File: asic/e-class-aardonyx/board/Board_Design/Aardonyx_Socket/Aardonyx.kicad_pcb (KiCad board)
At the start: 4 copper layers, 329 parts, among them J1 Conn_1x4, J10 Conn_1x3_M, J11 Conn_1x8, J12 Conn_1x3_M, J13 USB_B_6PIN, J14 Conn_1x4, J15 Conn_1x3_M, J16 USB_OTG, J17 Conn_1x8, J18 Conn_1x3_M, J19 Conn_1x3_M, J2 Conn_1x6, J3 Conn_1x10_F, J4 Conn_1x8_F, J5 Conn_1x8_F, J6 Conn_1x6_F, J7 Conn_1x3_M, J8 PJ-202H PWRJACK, J9 Conn_1x6, Q1 FDN339AN, SW1 FSM2JSMAATR, SW2 SW_DIP_x03, SW3 SW_SPST, U1 LSF0108PWR, U10 ADM1186, U11 FT2232H, U12 TPS7A7002DDAR, U13 TPS54627DDAR, U14 93LC56BT-I_OT, U15 TPS7A7002DDAR, U2 SKT32E, U3 IS42S32160F-TSOP2, U4 LSF0108PWR, U5 CDCE913PW, U6 ADC128S102CIMTX/NOPB, U7 74AUP1G09GW, U8 IS25LP256x-xM, U9 CAT24M01WI-GT3, Y1 27MHz, Y2 12MHz

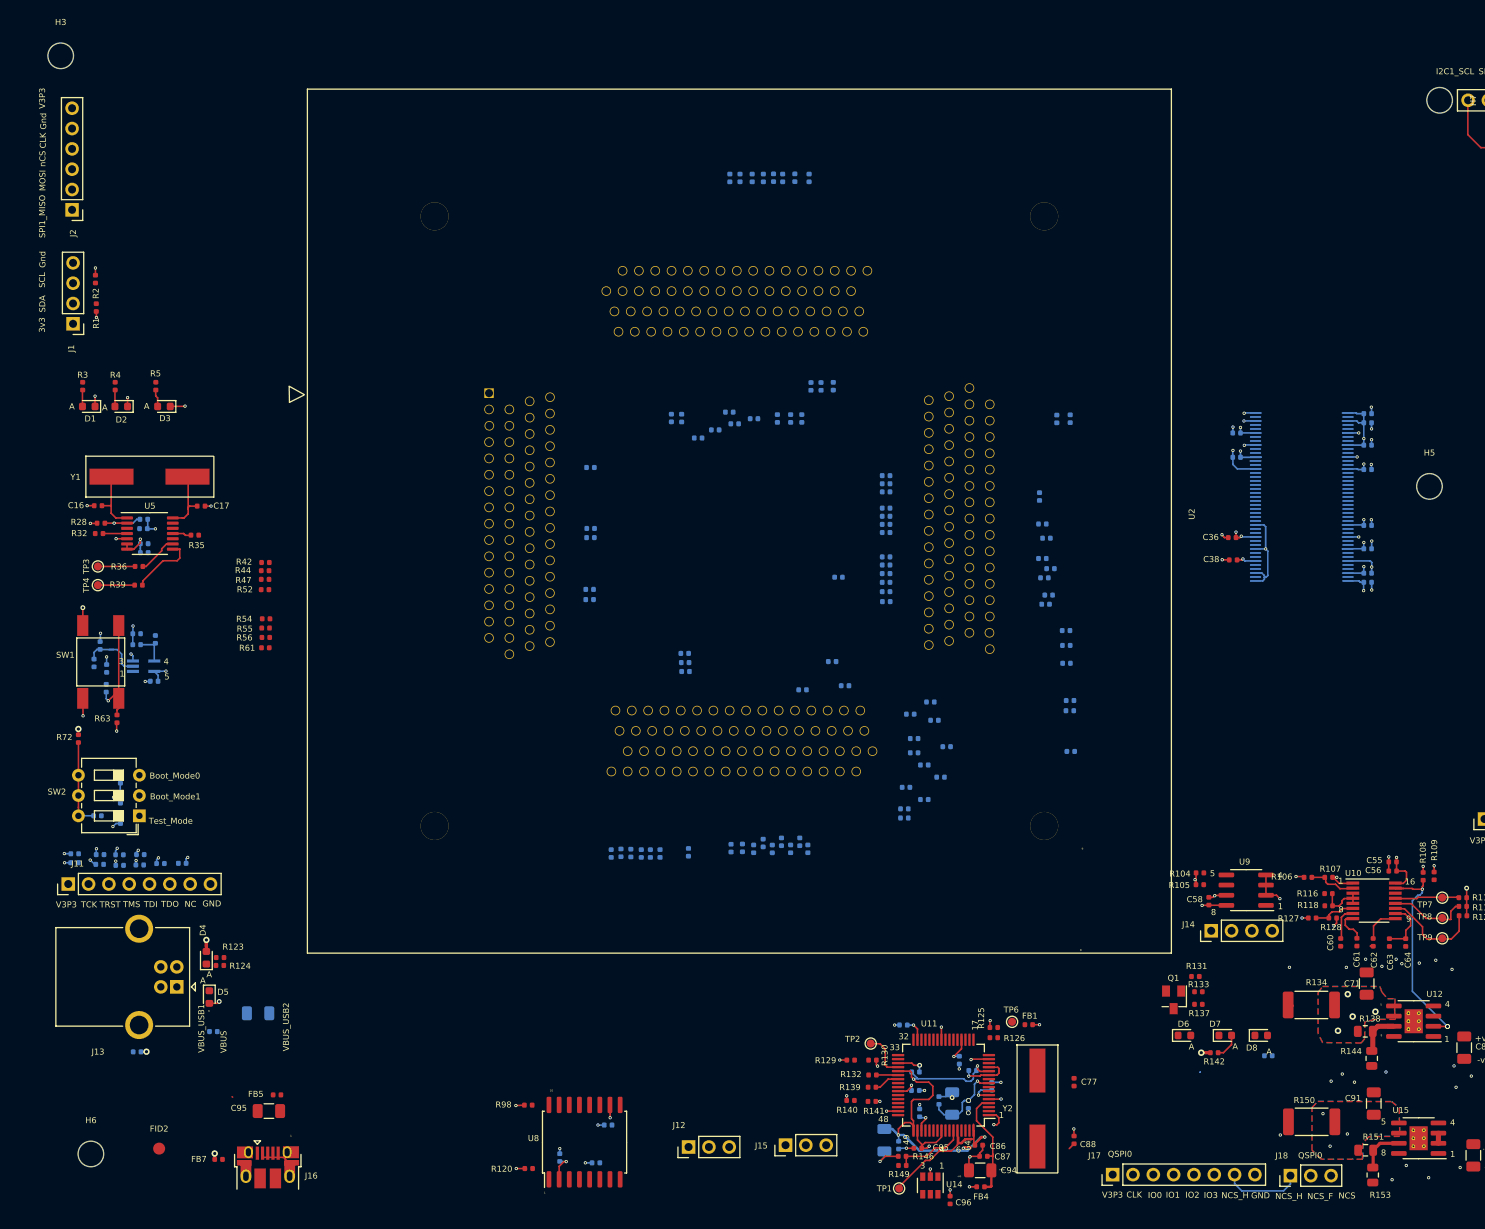
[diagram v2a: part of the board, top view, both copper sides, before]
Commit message: Adding Mounting hole
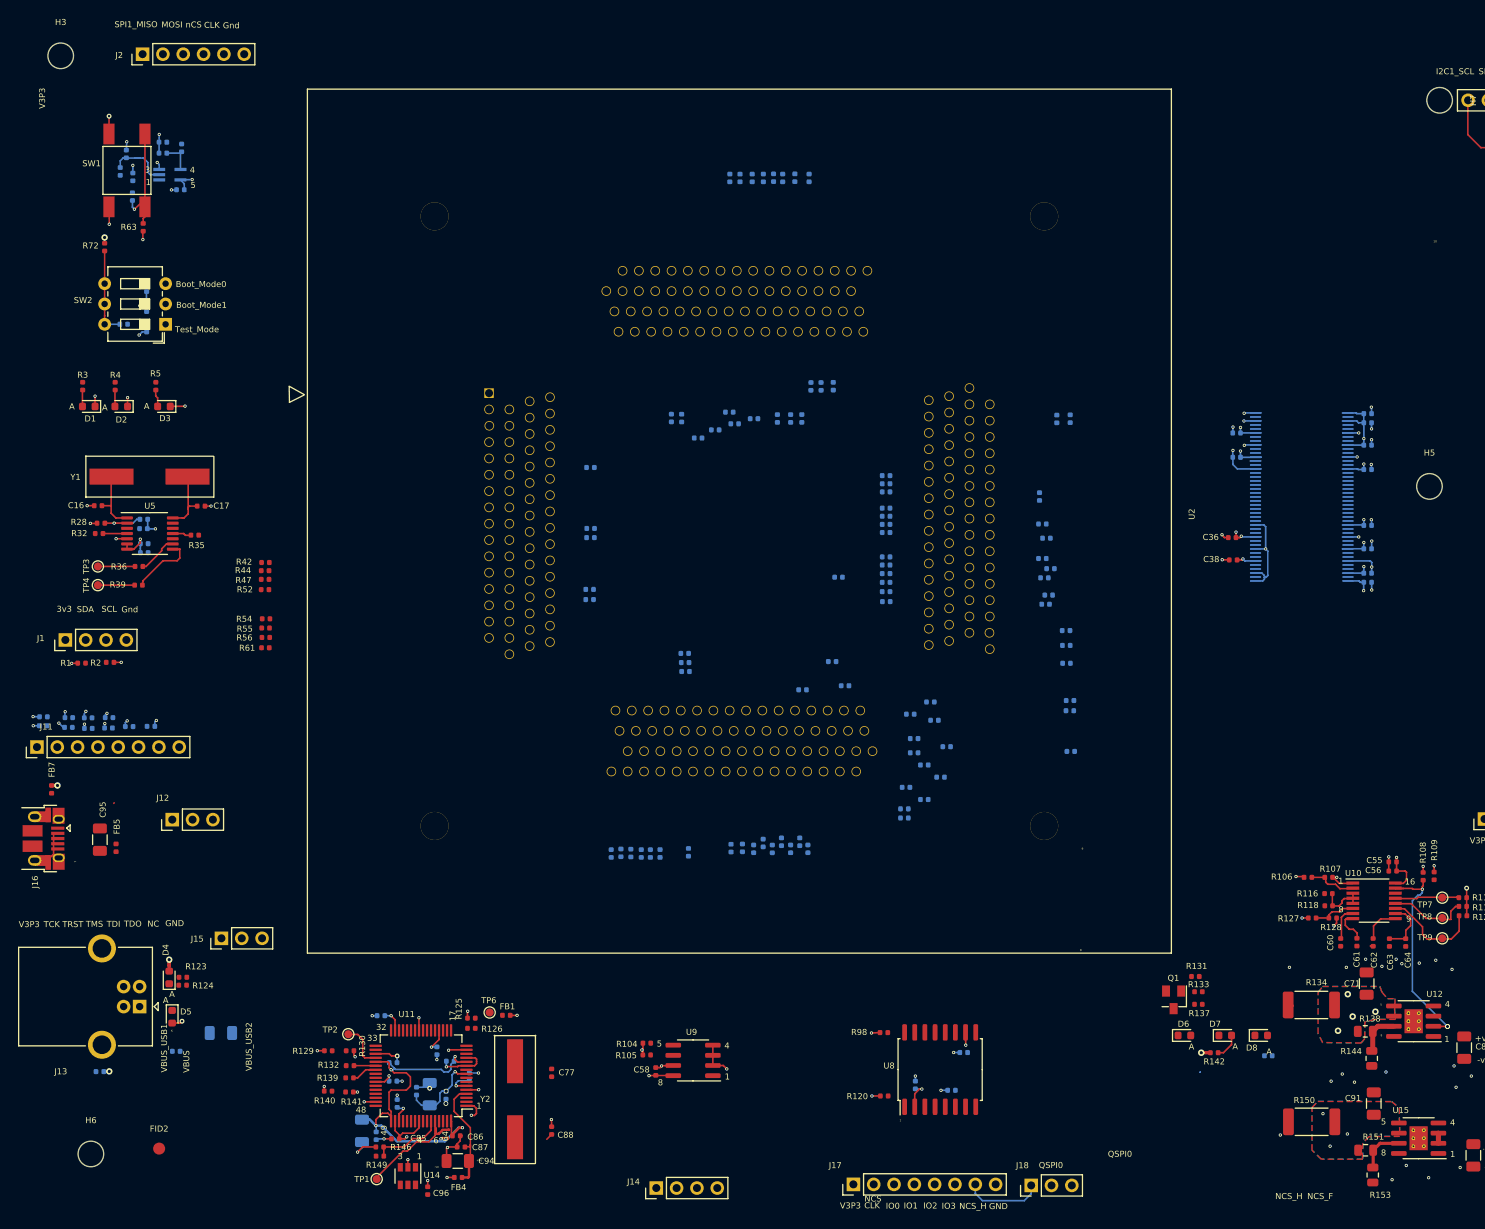
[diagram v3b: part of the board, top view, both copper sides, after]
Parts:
- moved J14 76.5 mm to (123.5, 159.3)
- moved J12 76.4 mm to (63.0, 113.2)
- moved J15 75.1 mm to (69.2, 128.1)
- moved R105 72.3 mm to (122.4, 142.6)
- moved U9 72.3 mm to (128.1, 143.3)
- moved C58 72.3 mm to (123.5, 144.7)
- moved R104 72.3 mm to (122.4, 141.2)
- moved C59 65.3 mm to (89.1, 137.7)
- moved C70 65.3 mm to (96.1, 142.1)
- moved C73 65.3 mm to (97.8, 143.4)
- moved C78 65.3 mm to (93.6, 147.2)
- moved C85 65.3 mm to (90.9, 153.1)
- moved C86 65.3 mm to (98.5, 152.8)
- moved C87 65.3 mm to (99.1, 154.2)
- moved FB1 65.3 mm to (104.8, 137.7)
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
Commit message: update sock track & foot prin soc th
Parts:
- moved R77 34.2 mm to (122.9, 112.3), turned to 270 degrees
- moved R76 29.9 mm to (124.6, 112.2), turned to 270 degrees
- moved C34 28.5 mm to (151.5, 73.1)
- moved C13 28.4 mm to (151.7, 89.0)
- moved C25 28.4 mm to (151.6, 82.6)
- moved C33 28.4 mm to (151.2, 75.7)
- moved C20 28.4 mm to (151.6, 83.9)
- moved C30 28.4 mm to (151.2, 77.9)
- moved R73 28.1 mm to (126.4, 112.2), turned to 270 degrees
- moved R66 27.5 mm to (169.3, 96.6), turned to 180 degrees
- moved R78 21.5 mm to (138.0, 112.2), turned to 270 degrees
- moved R22 21.5 mm to (168.7, 57.4)
- moved R26 20.6 mm to (169.0, 62.2)
- moved R25 20.1 mm to (168.7, 60.7)
- moved R27 20.0 mm to (169.0, 64.2)
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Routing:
- net /sdram/SDRAM_D16: track 0.00 -> 56.9 mm
- net /sdram/SDRAM_D18: track 0.00 -> 56.7 mm
- net /sdram/SDRAM_D20: track 0.00 -> 56.5 mm
- net /sdram/SDRAM_D17: track 0.00 -> 56.4 mm
- net /sdram/SDRAM_D19: track 0.00 -> 56.3 mm
- net /sdram/SDRAM_D22: track 0.00 -> 55.7 mm
- net /sdram/SDRAM_D23: track 0.00 -> 55.5 mm
- net /sdram/SDRAM_D21: track 0.00 -> 55.5 mm
- net Net-(R26-Pad2): track 0.00 -> 9.53 mm
- net Net-(R25-Pad2): track 0.00 -> 9.29 mm

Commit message: updated soc track
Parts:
- moved C2 48.1 mm to (167.4, 15.5)
- moved C3 48.1 mm to (169.0, 15.4)
- moved R24 29.3 mm to (136.6, 37.3)
- moved R23 28.8 mm to (133.0, 35.8)
- moved R13 27.9 mm to (150.7, 58.0), turned to 0 degrees
- moved R21 27.2 mm to (139.9, 37.3)
- moved R11 25.7 mm to (150.6, 56.8), turned to 0 degrees
- moved R79 24.3 mm to (141.9, 111.8), turned to 270 degrees
- moved R10 24.0 mm to (150.6, 55.6), turned to 0 degrees
- moved R17 23.0 mm to (153.9, 42.1), turned to 0 degrees
- moved R94 22.7 mm to (140.8, 111.8), turned to 270 degrees
- moved R16 19.3 mm to (151.8, 40.6), turned to 0 degrees
- moved R7 19.0 mm to (153.9, 43.5), turned to 180 degrees
- moved C15 17.8 mm to (205.8, 50.0)
- moved C21 17.4 mm to (205.7, 53.4)
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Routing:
- net /sdram/SDRAM_A10: track 0.00 -> 108.4 mm, vias 0 -> 2
- net /sdram/SDRAM_A11: track 0.00 -> 107.3 mm, vias 0 -> 2
- net /sdram/SDRAM_A12: track 0.00 -> 106.8 mm, vias 0 -> 2
- net /sdram/SDRAM_A9: track 0.00 -> 102.4 mm, vias 0 -> 2
- net /sdram/SDRAM_A8: track 0.00 -> 99.9 mm, vias 0 -> 2
- net /sdram/SDRAM_A2: track 0.00 -> 98.7 mm, vias 0 -> 2
- net /sdram/SDRAM_A1: track 0.00 -> 97.8 mm, vias 0 -> 2
- net /sdram/SDRAM_A7: track 0.00 -> 97.1 mm, vias 0 -> 2
- net /sdram/SDRAM_A0: track 0.00 -> 96.3 mm, vias 0 -> 2
- net /sdram/SDRAM_A6: track 0.00 -> 94.3 mm, vias 0 -> 2
- net /sdram/SDRAM_A5: track 0.00 -> 91.2 mm, vias 0 -> 2
- net /sdram/SDRAM_A4: track 0.00 -> 88.1 mm, vias 0 -> 2
- net /sdram/SDRAM_A3: track 0.00 -> 84.9 mm, vias 0 -> 2
- net /sdram/SDRAM_DQM0: track 0.00 -> 82.9 mm, vias 0 -> 2
- net /sdram/SDRAM_CLK: track 0.00 -> 80.2 mm, vias 0 -> 2
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- added copper zone on In1.Cu, net GND

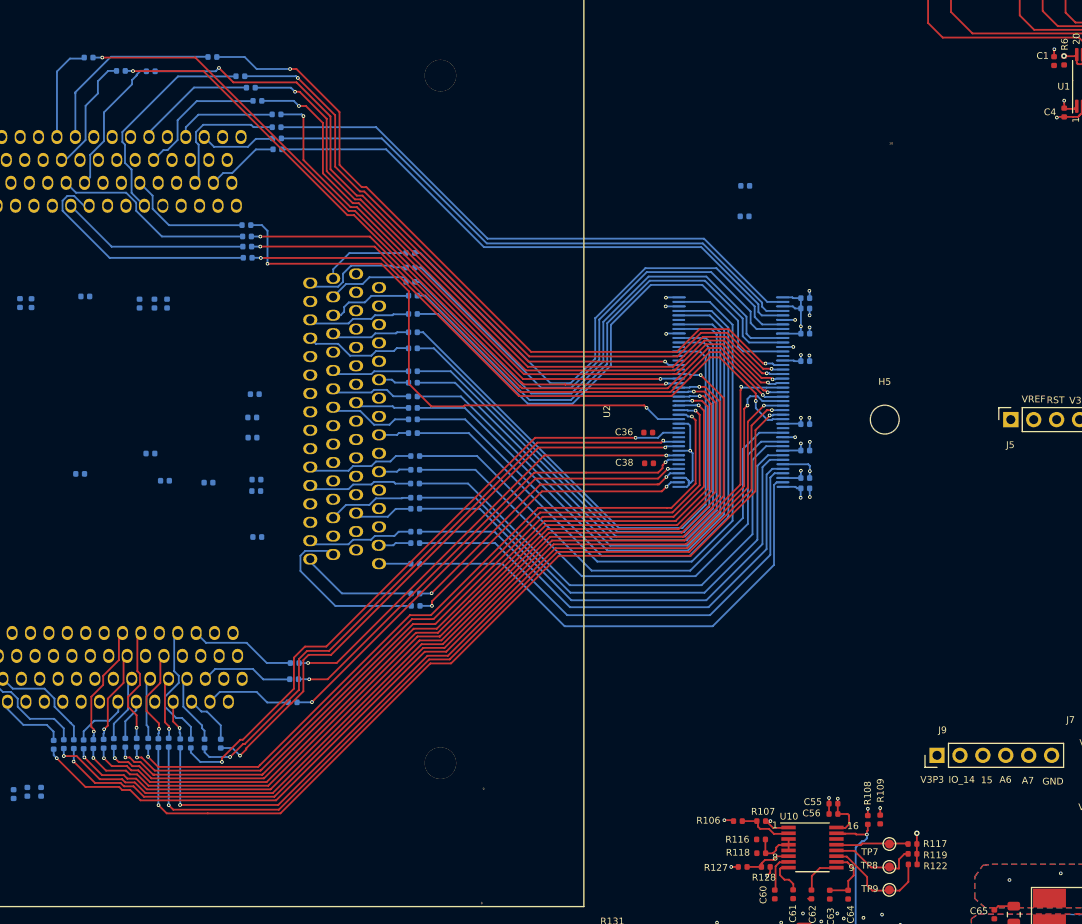
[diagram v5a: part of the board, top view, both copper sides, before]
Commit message: SDRAM Routing with Machine socket
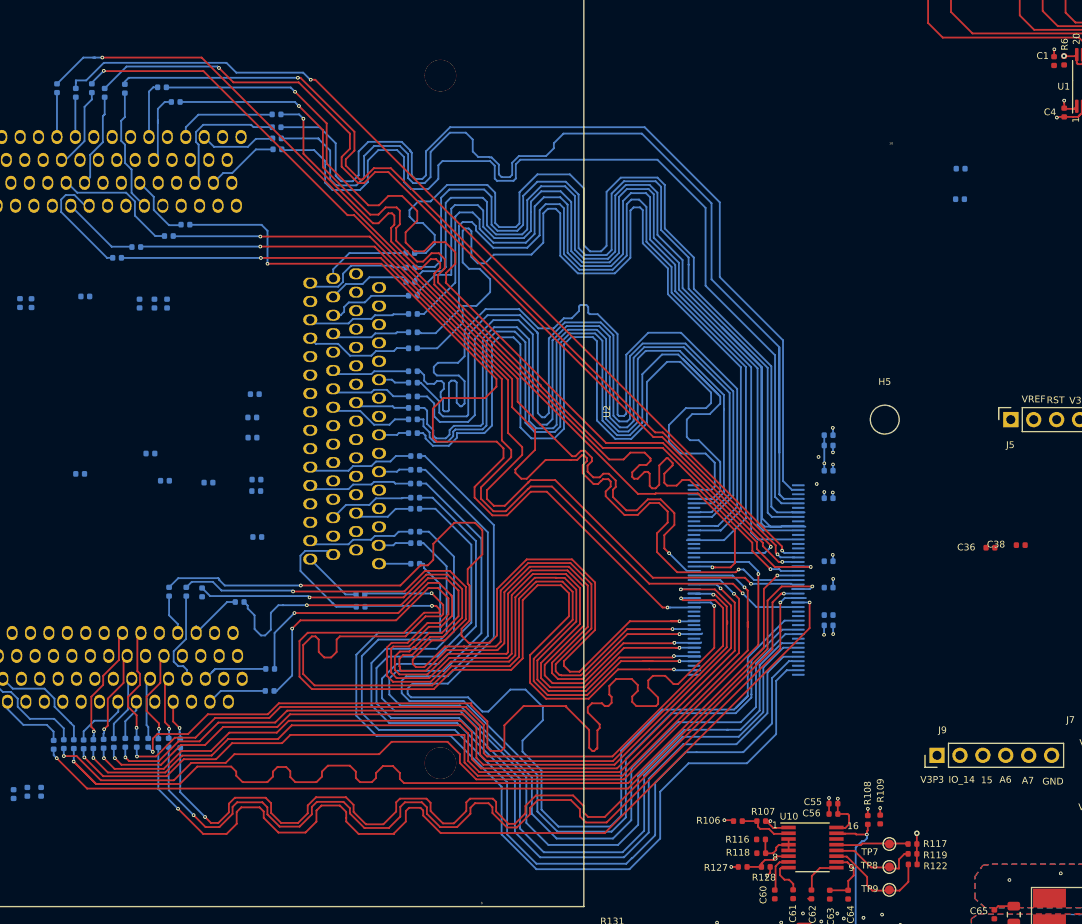
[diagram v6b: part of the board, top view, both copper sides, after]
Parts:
- moved C38 42.2 mm to (236.4, 89.9)
- moved C36 40.0 mm to (233.0, 90.1)
- moved C15 24.0 mm to (229.7, 48.1)
- moved C21 24.0 mm to (229.6, 51.5)
- moved U3 20.9 mm to (205.9, 93.7)
- moved R74 17.0 mm to (142.0, 95.0), turned to 270 degrees
- moved R71 17.0 mm to (143.9, 95.0), turned to 270 degrees
- moved R68 16.9 mm to (145.6, 95.1), turned to 270 degrees
- moved R12 15.6 mm to (131.6, 39.7), turned to 90 degrees
- moved C18 15.4 mm to (215.1, 81.6)
- moved C26 15.4 mm to (215.1, 84.7)
- moved C35 15.4 mm to (215.1, 91.6)
- moved C40 15.4 mm to (215.1, 97.6)
- moved C43 15.4 mm to (215.1, 94.6)
- moved C45 15.4 mm to (215.1, 98.8)
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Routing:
- net /sdram/SDRAM_D25: track 34.7 -> 106.8 mm
- net /sdram/SDRAM_D5: track 58.3 -> 129.9 mm
- net /sdram/SDRAM_D24: track 35.2 -> 101.7 mm
- net /sdram/SDRAM_D16: track 56.9 -> 113.7 mm
- net /sdram/SDRAM_D1: track 64.4 -> 120.7 mm
- net /sdram/SDRAM_D28: track 52.2 -> 105.8 mm
- net /sdram/SDRAM_D26: track 53.5 -> 103.1 mm
- net /sdram/SDRAM_D27: track 53.0 -> 101.8 mm
- net /sdram/SDRAM_D20: track 56.5 -> 104.5 mm
- net /sdram/SDRAM_D19: track 56.3 -> 103.3 mm
- net /sdram/SDRAM_D18: track 56.7 -> 103.1 mm
- net /sdram/SDRAM_D22: track 55.7 -> 101.9 mm
- net /sdram/SDRAM_D3: track 58.5 -> 104.7 mm
- net /sdram/SDRAM_D17: track 56.4 -> 102.4 mm
- net /sdram/SDRAM_D21: track 55.5 -> 100.8 mm
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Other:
- board text removed: "43"
- board text removed: "44"
- board text removed: "86"

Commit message: updated soc track
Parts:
- R81, R82, R83, R84, R85, R86: moved to F.Cu
- moved D1 55.2 mm to (79.5, 13.3)
- moved D2 55.2 mm to (83.6, 13.3)
- moved D3 55.2 mm to (88.9, 13.3)
- moved R5 51.3 mm to (88.1, 15.4), turned to 90 degrees
- moved R4 51.3 mm to (82.7, 15.3), turned to 90 degrees
- moved R3 51.1 mm to (78.7, 15.5), turned to 90 degrees
- moved R83 23.3 mm to (121.3, 133.1)
- moved C2 22.3 mm to (145.2, 18.2)
- moved C3 22.3 mm to (146.9, 18.2)
- moved R82 21.3 mm to (118.8, 133.1)
- moved R85 21.1 mm to (122.7, 133.1)
- moved R84 21.0 mm to (120.0, 133.2)
- moved R86 21.0 mm to (123.9, 133.1)
- moved R81 20.9 mm to (117.7, 133.1)
- moved C21 13.6 mm to (238.2, 40.9)
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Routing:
- net /arduino_header/RESET_AH: track 0.00 -> 313.1 mm, vias 0 -> 2
- net /arduino_header/IO_15: track 0.00 -> 259.6 mm, vias 0 -> 2
- net /arduino_header/IO_14: track 0.00 -> 255.3 mm, vias 0 -> 2
- net /arduino_header/SPI0_nCS: track 0.00 -> 248.8 mm, vias 0 -> 2
- net /arduino_header/SPI0_MISO: track 0.00 -> 248.0 mm, vias 0 -> 2
- net /arduino_header/SPI0_CLK: track 0.00 -> 246.9 mm, vias 0 -> 2
- net /arduino_header/SPI0_MOSI: track 0.00 -> 246.8 mm, vias 0 -> 2
- net /power_2/RESET_ASIC: track 0.00 -> 236.7 mm, vias 0 -> 3
- net /arduino_header/IO_13: track 0.00 -> 223.1 mm, vias 0 -> 1
- net VBUS: track 0.00 -> 188.0 mm, vias 0 -> 1
- net /arduino_header/I2C1_SDA: track 0.00 -> 186.8 mm, vias 0 -> 2
- net /RESET: track 0.00 -> 186.5 mm, vias 0 -> 1
- net /arduino_header/I2C1_SCL: track 0.00 -> 184.2 mm, vias 0 -> 2
- net /arduino_header/IO_12: track 0.00 -> 174.3 mm
- net /arduino_header/IO_11: track 0.00 -> 174.1 mm
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
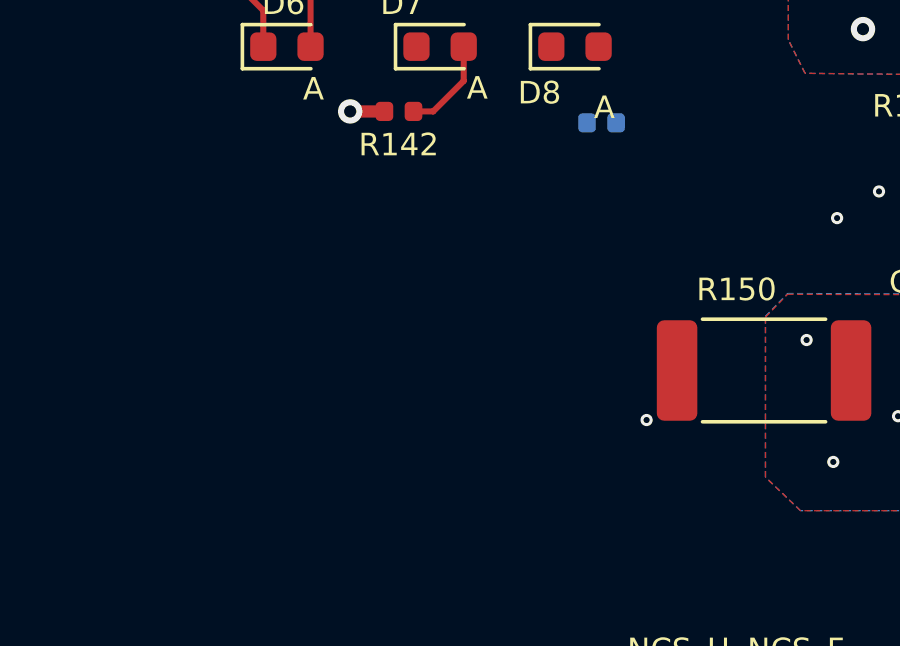
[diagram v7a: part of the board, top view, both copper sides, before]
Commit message: Updating power layer
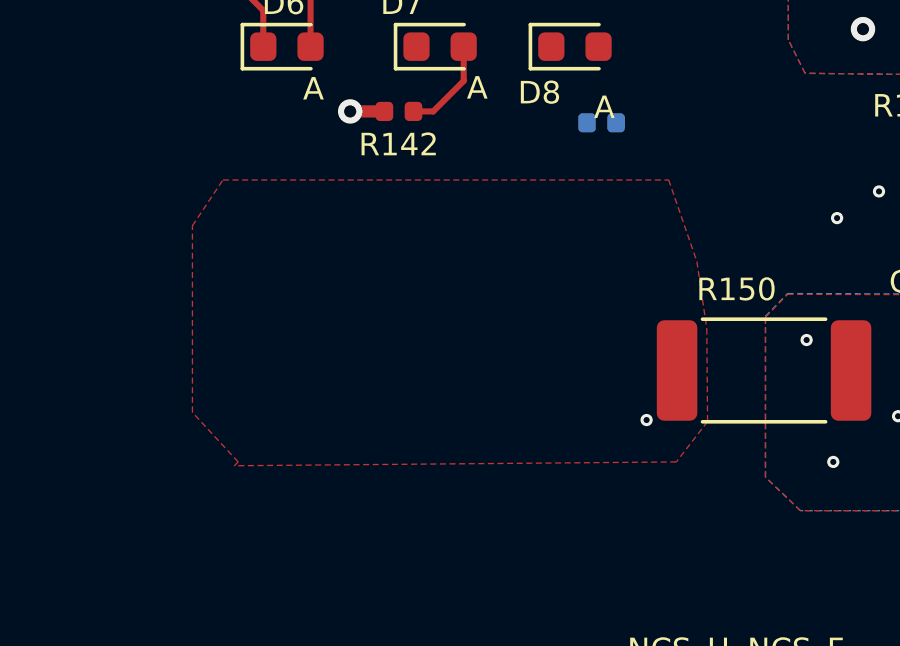
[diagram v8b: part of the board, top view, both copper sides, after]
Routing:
- added copper zone on F.Cu, net V3P3
